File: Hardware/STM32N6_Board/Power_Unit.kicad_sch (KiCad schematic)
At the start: 71 parts, among them J1 Conn_01x02_Pin, U1 STM32N657I0H3Q, U2 SPX5205-ADJ, U3 SPX5205-ADJ, U4 SPX5205-ADJ, U5 SPX5205-ADJ, U6 MC34064-ADJ-TR

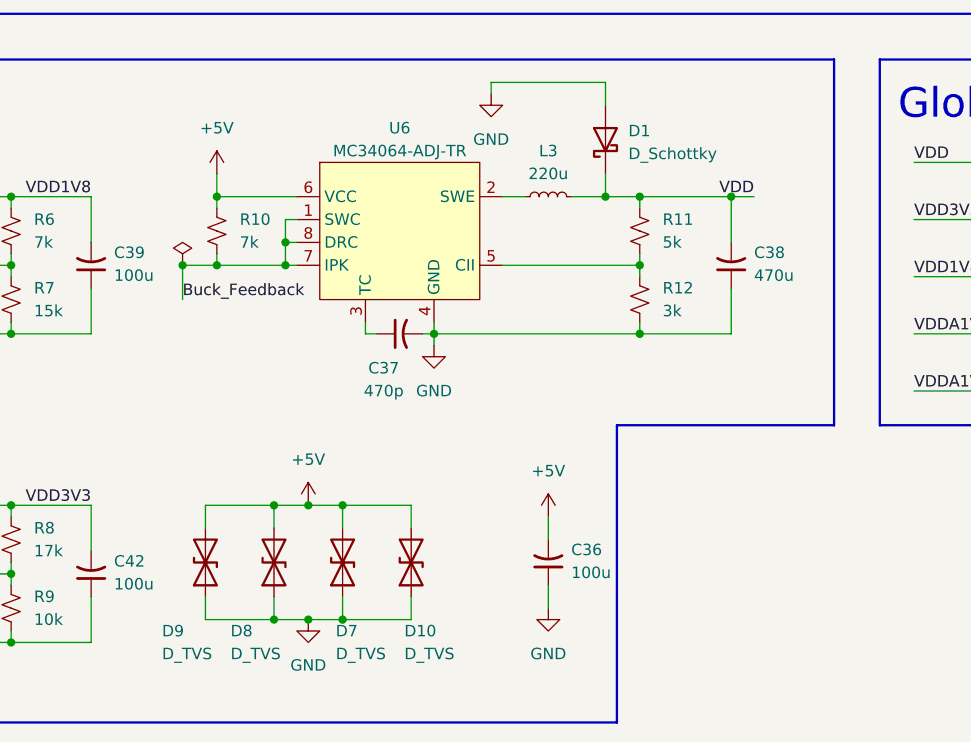
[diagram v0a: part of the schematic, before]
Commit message: Added the gerbers, drill files, BOM, and CPL files
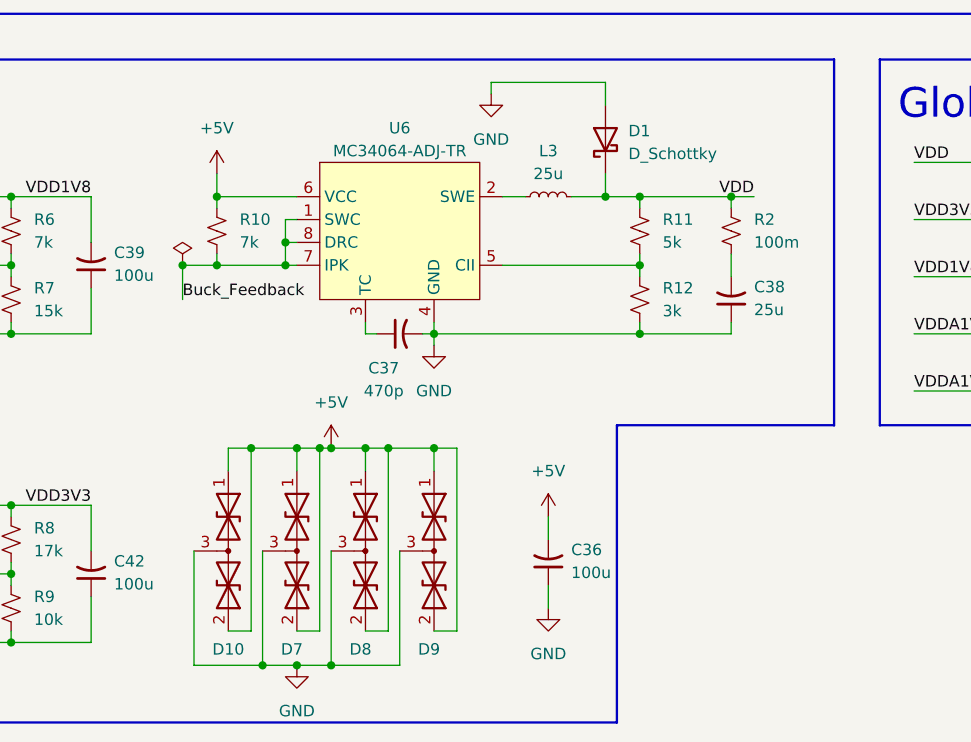
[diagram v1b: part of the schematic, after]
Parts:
- removed D10, D7, D8, D9: D_TVS, LED_SMD:LED_0805_2012Metric_Pad1.15x1.40mm_HandSolder, symbol Device:D_TVS
- added D10, D7, D8, D9: D_TVS_Dual_AAC, Package_TO_SOT_SMD:SOT-723, symbol Device:D_TVS_Dual_AAC
- added R2: 100m, Resistor_SMD:R_0805_2012Metric_Pad1.20x1.40mm_HandSolder, symbol Device:R_Small_US
- C38: value 470u -> 25u
- L3: value 220u -> 25u
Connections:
- net +5V: now also D10.1 (A1), D10.2 (A2), D7.1 (A1), D7.2 (A2), D8.1 (A1), D8.2 (A2), D9.1 (A1), D9.2 (A2)
- net GND: now also D10.3 (common), D7.3 (common), D8.3 (common), D9.3 (common)
- net VDD: now also R2.1; no longer C38.2
- new net: C38.2, R2.2
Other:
- moved on the sheet: C38
